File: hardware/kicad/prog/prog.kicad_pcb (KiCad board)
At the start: 4 copper layers, 174 x 134 mm, 123 parts, among them J1 AES_PROG, J2 Câble PROG-CHA, J3 CONF P, J4 CONF V, U1 AMS1117-3.3, U10 iCE40HX4K-TQ144, U11 W9825G6KH-6, U12 iCE40HX4K-TQ144, U13 W9825G6KH-6, U2 AP2112K-1.2, U3 74LVC16244A, U4 74LVC16244A, U5 74LVC16244A, U6 74LVC16245A, U7 74LVC16245A, U8 74AHCT125, U9 74LVC1G07, X1 25 MHz 3,3 V, X2 25 MHz 3,3 V

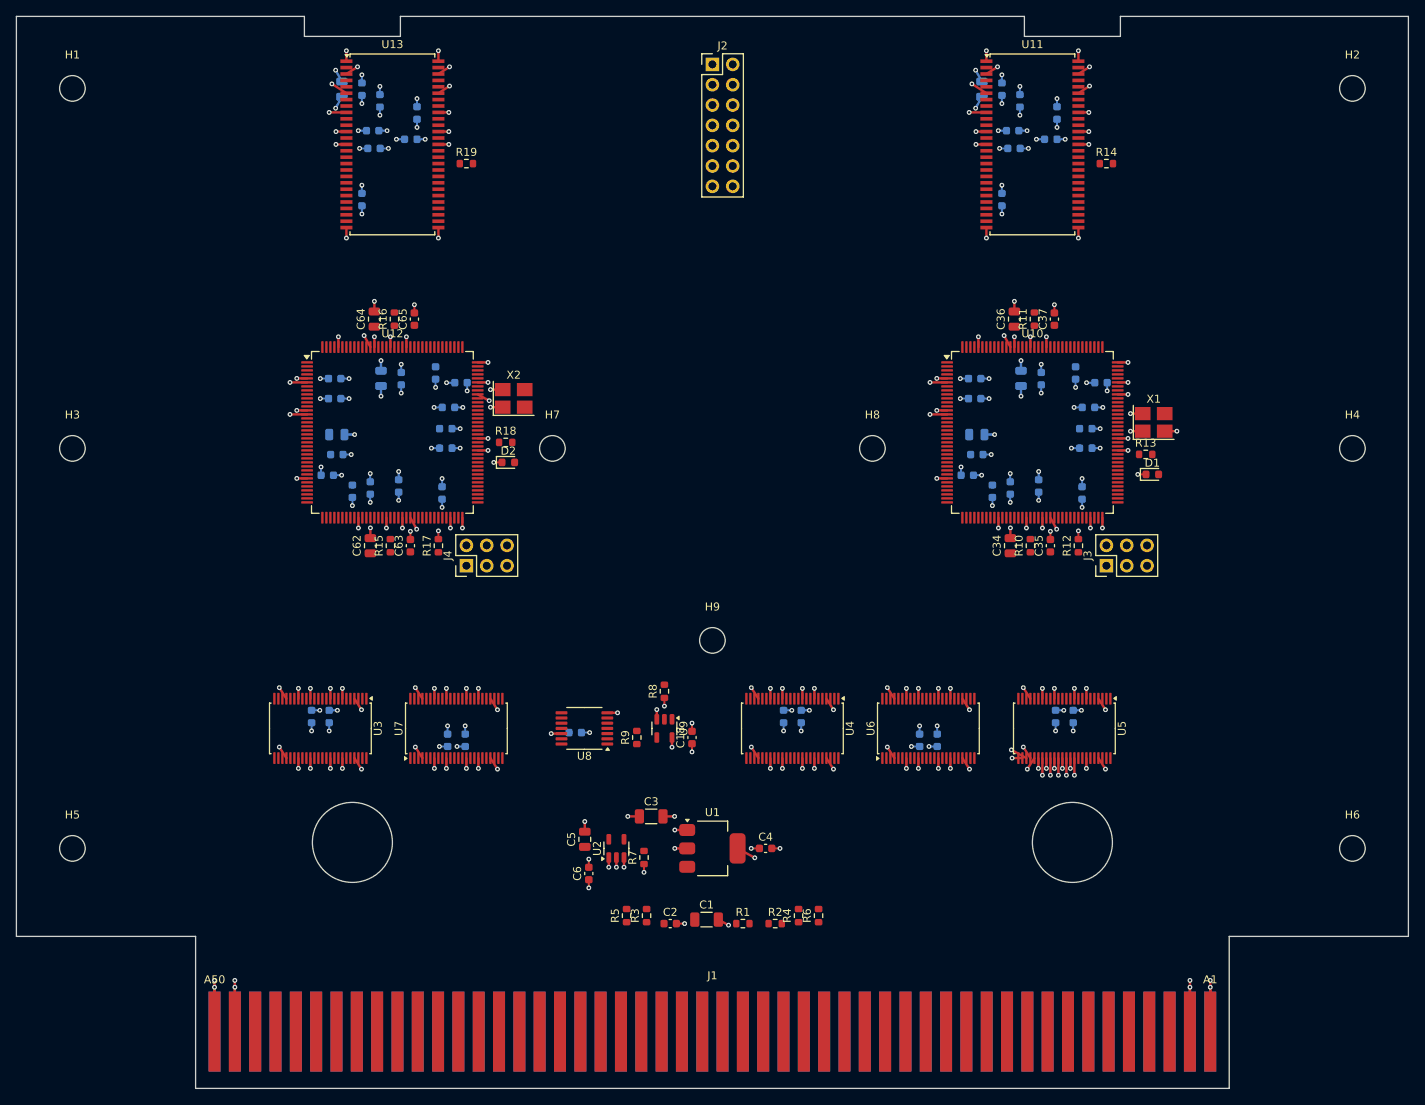
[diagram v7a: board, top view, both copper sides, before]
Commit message: PCB : vias vers les plans réglementaires et hors des couloirs de sortie
Le routage précédent (171 liaisons non routées, 40 violations dès le
départ) était faussé par les vias vers les plans : posés vers
l'extérieur des boîtiers, ils bloquaient la sortie des signaux, et leur
piste de raccordement pouvait frôler les pastilles voisines.
- direction suivant l'axe de la pastille (et non le centre du
  composant, faux près des coins et sur le connecteur de bord) ;
- QFP et SO : via sous le boîtier d'abord ; jamais sous le Pico ;
- via et piste vérifiés à 0,127 mm de tout autre réseau ;
- plans prolongés dans la languette (vias des contacts de masse).
DRC des cartes préparées : aucune violation de règle.

Co-Authored-By: Claude Opus 5.5 <noreply@anthropic.com>
Claude-Session: https://claude.ai/code/session_01WKfXP1YJ8otGxZ5dsY6Agh
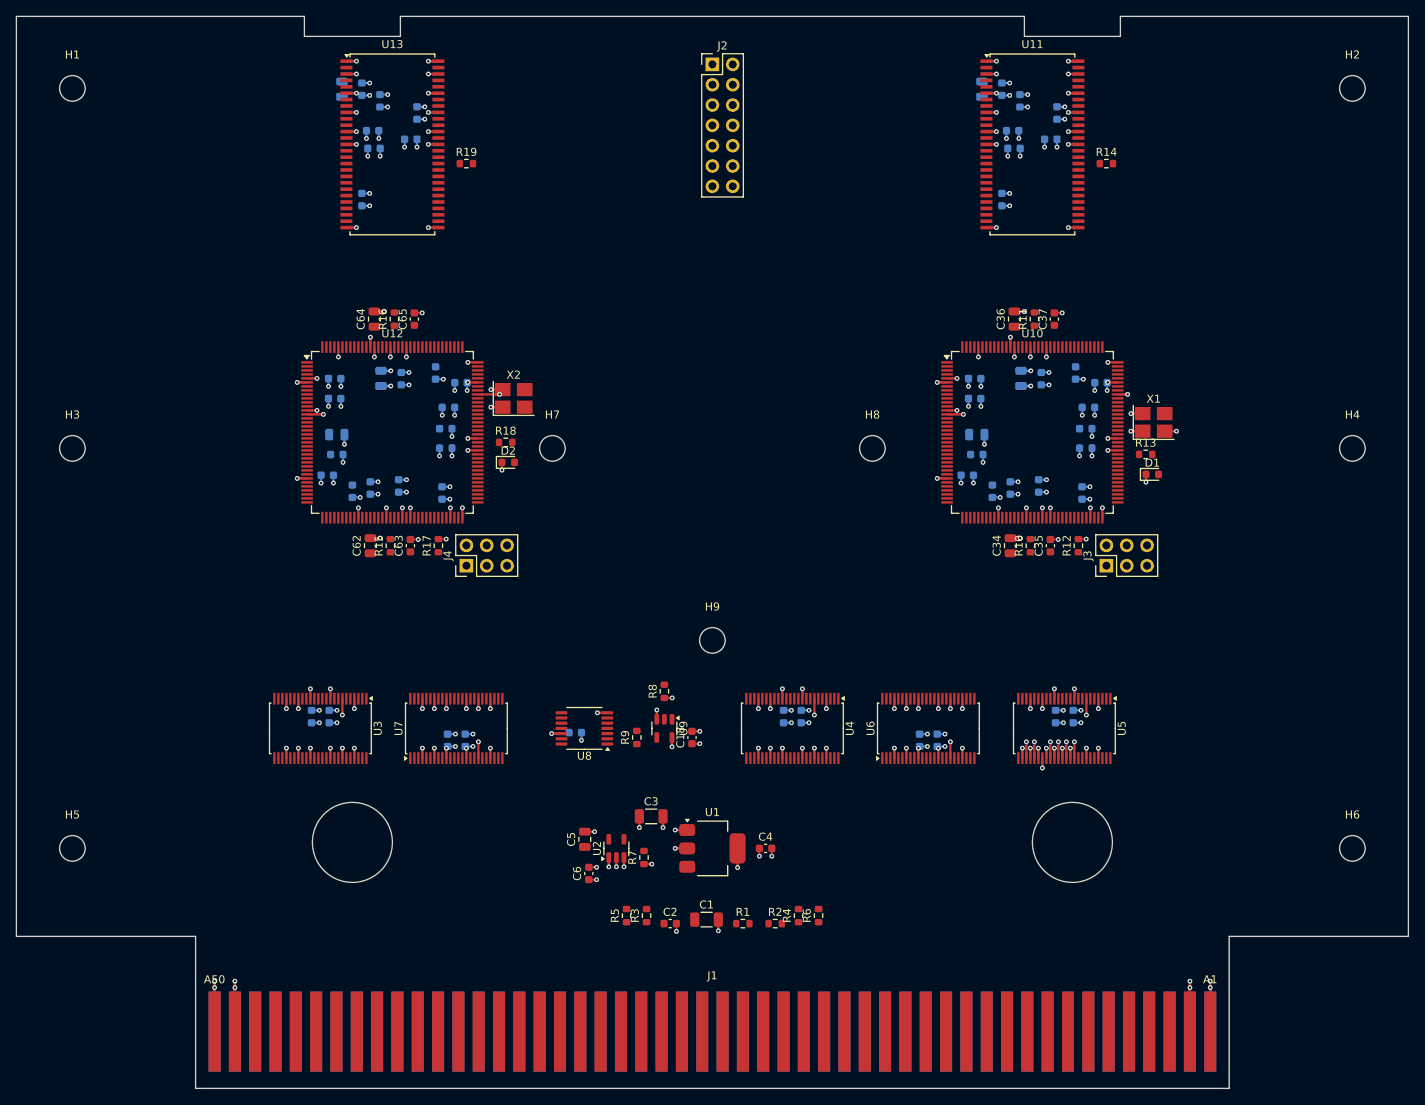
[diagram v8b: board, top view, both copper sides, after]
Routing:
- net GND: track 268.2 -> 245.2 mm, vias 178 -> 176
- net +3V3: track 147.0 -> 137.5 mm, vias 117 -> 115
